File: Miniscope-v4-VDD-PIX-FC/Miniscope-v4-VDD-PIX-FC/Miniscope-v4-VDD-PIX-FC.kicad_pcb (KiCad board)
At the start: 2 copper layers, 7.2 x 6.5 mm, 7 parts, among them J1 Conn_01x01, J2 Conn_01x01, J3 Conn_01x01, U1 MCP1711

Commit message: Add pad labels on bottom silkscreen
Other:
- board text added: "5V"
- board text added: "GND"
- board text added: "V_PIX"
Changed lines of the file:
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@@
   (general
     (thickness 0.381)
-    (drawings 13)
+    (drawings 17)
     (tracks 19)
     (zones 0)
@@
     )
   )
+  (gr_line (start 150.25 97) (end 150.25 98) (layer B.SilkS) (width 0.12))
+  (gr_text V_PIX (at 149 98.75) (layer B.SilkS)
+    (effects (font (size 0.8 0.8) (thickness 0.1)) (justify mirror))
+  )
+  (gr_text GND (at 147.25 97.5) (layer B.SilkS)
+    (effects (font (size 0.8 0.8) (thickness 0.1)) (justify mirror))
+  )
+  (gr_text 5V (at 145 98 270) (layer B.SilkS)
+    (effects (font (size 0.8 0.8) (thickness 0.1)) (justify mirror))
+  )
   (gr_text "Should have min 15mil edge clearance" (at 167.75 97.75) (layer Cmts.User)

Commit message: Finalize v0.1 VDD-PIX FC for fab at OSHPark and PCBWay
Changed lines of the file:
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@@
   (general
     (thickness 0.381)
-    (drawings 17)
+    (drawings 20)
     (tracks 19)
     (zones 0)
@@
     (visible_elements FFFFFF7F)
     (pcbplotparams
-      (layerselection 0x010fc_ffffffff)
+      (layerselection 0x018fc_ffffffff)
       (usegerberextensions false)
       (usegerberattributes true)
@@
 ) (width 0))
       ))
+    (model ${KICAD_AHARONI_LAB}/Modules/Package_QFN.pretty/MCP1711.step
+      (at (xyz 0 0 0))
+      (scale (xyz 1 1 1))
+      (rotate (xyz -90 0 0))
+    )
   )
   (module .Connector:Conn_1x1_700_Circular_Pad (layer F.Cu)
@@
     )
   )
+  (gr_line (start 144 97) (end 144 101) (layer Eco2.User) (width 0.15))
+  (gr_line (start 151.25 97) (end 144 97) (layer Eco2.User) (width 0.15))
+  (gr_line (start 151.25 101) (end 151.25 97) (layer Eco2.User) (width 0.15))
+  (gr_line (start 144 101) (end 151.25 101) (layer Eco2.User) (width 0.15))
   (gr_line (start 150.25 97) (end 150.25 98) (layer B.SilkS) (width 0.12))
   (gr_text V_PIX (at 149 98.75) (layer B.SilkS)
@@
     (effects (font (size 1 1) (thickness 0.15)))
   )
-  (gr_line (start 148.8516 95.8276) (end 148.8516 96.0776) (layer F.SilkS) (width 0.12))
+  (gr_line (start 148.8516 95.8276) (end 148.8516 96.8276) (layer F.SilkS) (width 0.12))
   (gr_line (start 150.8516 95.8276) (end 148.8516 95.8276) (layer F.SilkS) (width 0.12))
   (gr_line (start 150.8516 99.3276) (end 150.8516 95.8276) (layer F.SilkS) (width 0.12))
   (gr_line (start 144.3516 96.8276) (end 144.3516 99.3276) (layer F.SilkS) (width 0.12))
-  (gr_line (start 148.8516 96.0776) (end 148.8516 96.8276) (layer F.SilkS) (width 0.12))
   (gr_line (start 148.8516 96.8276) (end 144.3516 96.8276) (layer F.SilkS) (width 0.12))
   (gr_line (start 150.8516 99.3276) (end 144.3516 99.3276) (layer F.SilkS) (width 0.12))

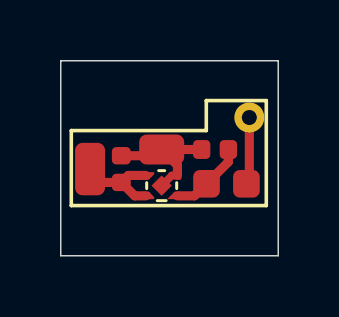
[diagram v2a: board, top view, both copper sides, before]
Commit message: Update hotfix VDD_PIX PC to v1.0
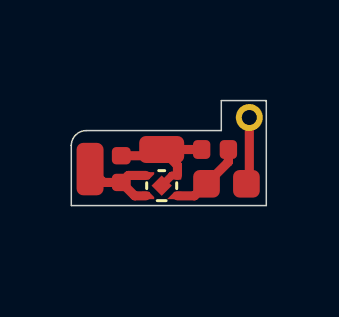
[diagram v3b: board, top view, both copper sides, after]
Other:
- board size 7.2 x 6.5 mm -> 6.5 x 3.5 mm
- board text added: "Dwgs.User holds larger board outline which requires manual cutting"
- board text added: "Eco2.User holds tape outline"
- board text removed: "OSHPark min size is 6.5mm x 6.5mm"
- board text removed: "Should have min 15mil edge clearance"
- board text removed: "V_PIX"

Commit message: Expand silkscreen openning for VDD_PIX Hotfix PC
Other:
- rule pad_to_mask_clearance: 0.05 -> 0.0762

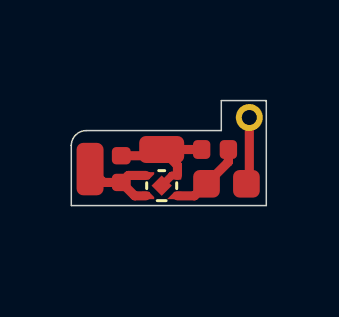
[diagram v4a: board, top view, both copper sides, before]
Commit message: Update 3.3V regulator for hotfix PC
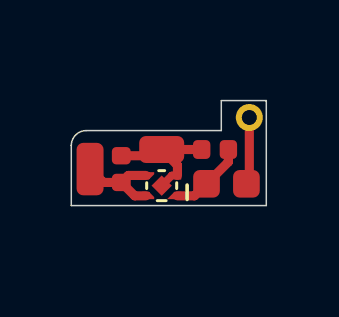
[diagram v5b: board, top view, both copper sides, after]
